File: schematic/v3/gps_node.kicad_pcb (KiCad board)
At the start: 2 copper layers, 48 x 75 mm, 81 parts, among them IC1 MCP73831/2, J1 Mounting Hole, J11 AVR ICSP, J12 UART RF, J13 LIPO_BAT, J15 UART GPS, J16 FW_UPDATE, J17 u.FL connector, J2 Mounting Hole, J3 Mounting Hole, J4 Mounting Hole, J5 TEST Vbatt, J6 USB_OTG, J7 Test 3.3v, J8 Test Gnd, J9 Test V_bak, SW1 RS stock no. 448-0747, SW2 SW_Push, SW3 SW_Push, U1 TLV71333PDBV, U2 ublox-cam-m8q-0, U3 TLV71333PDBV, U4 ATMEGA32U4-AU, U5 RN2483, U6 LIS3DH, Y1 16MHz

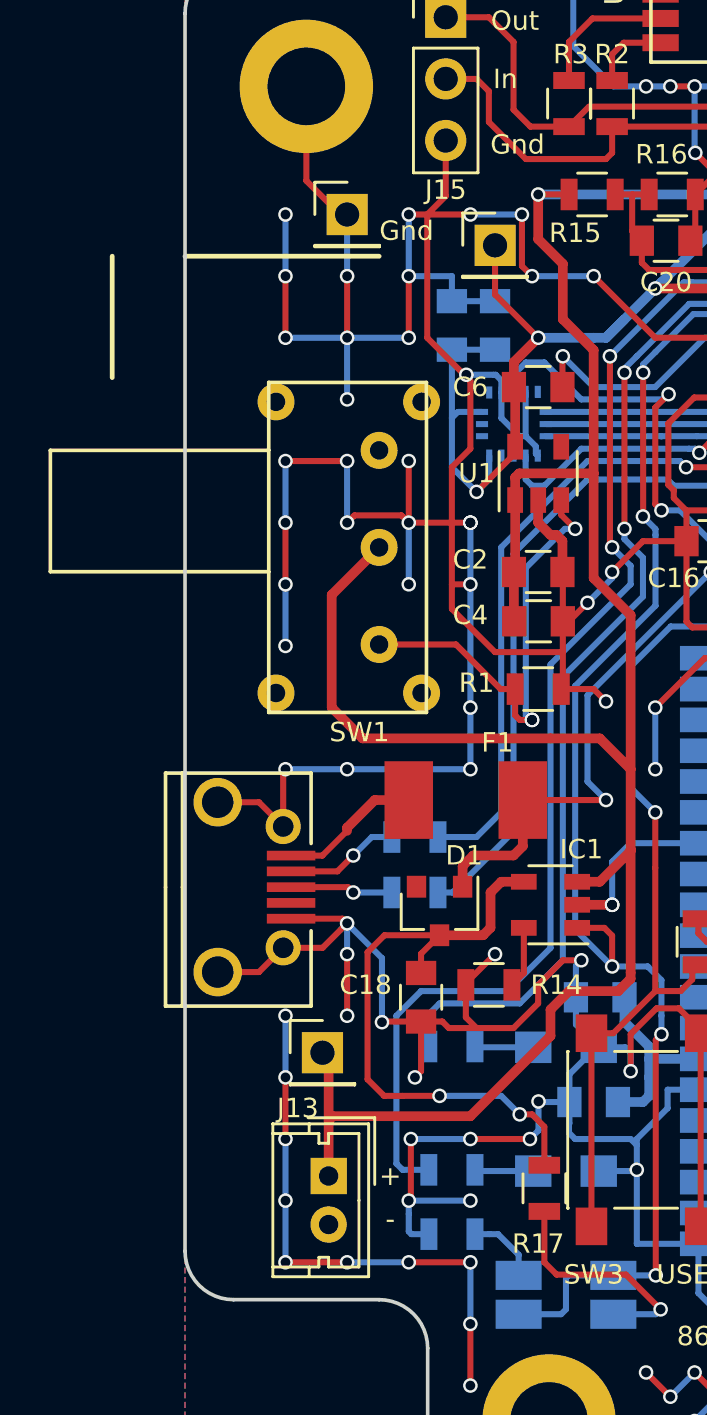
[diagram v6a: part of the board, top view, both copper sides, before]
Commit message: Moved usb connector
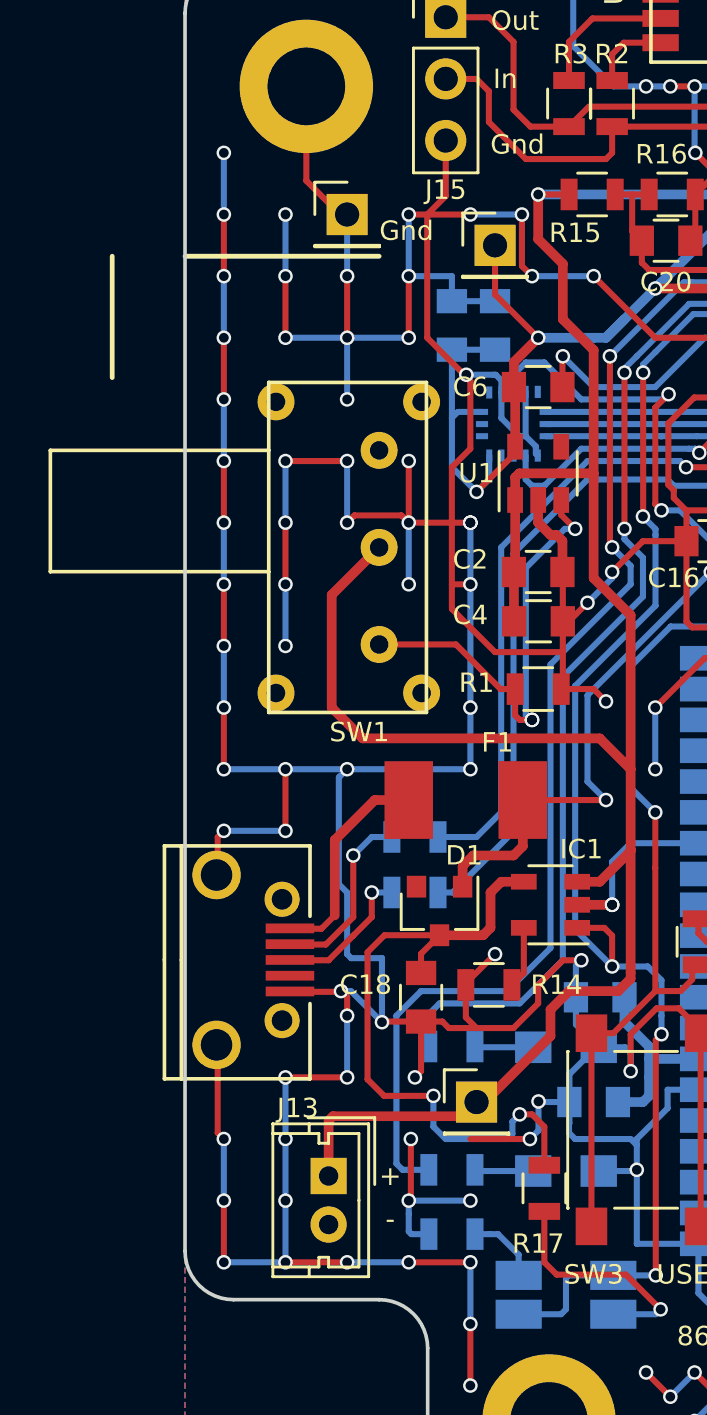
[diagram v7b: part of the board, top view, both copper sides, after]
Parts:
- moved J5 6.67 mm to (112.0, 117.9)
- moved J6 3.00 mm to (104.0, 112.0)
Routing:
- net GND: track 776.7 -> 817.9 mm, vias 230 -> 244
- net V_BATT: track 124.3 -> 116.6 mm
- net Net-(F1-Pad2): track 5.87 -> 8.86 mm
- net Net-(J6-Pad2): track 4.74 -> 7.48 mm
- net /power/V_Charger: track 25.3 -> 27.2 mm
- net Net-(J6-Pad3): track 4.24 -> 5.91 mm

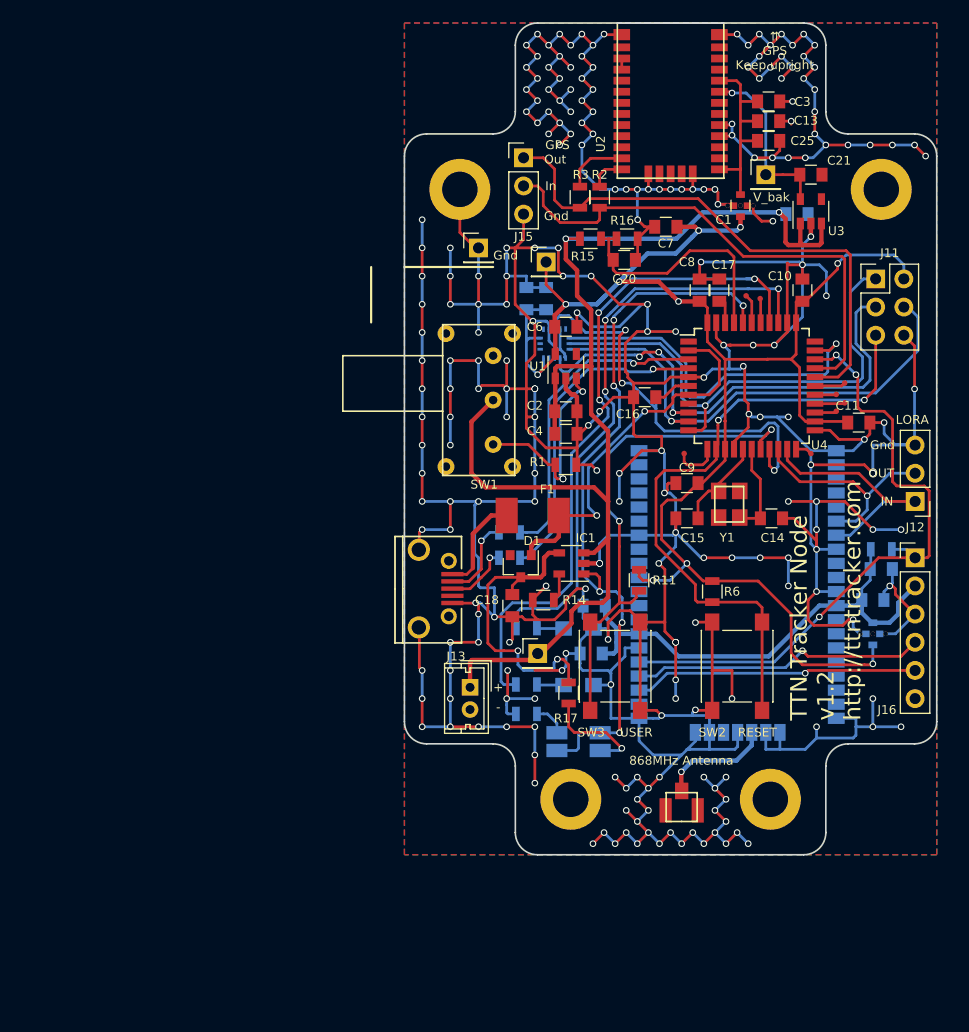
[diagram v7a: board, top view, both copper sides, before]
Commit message: Updated layout to revised schematic, moved switch and usb
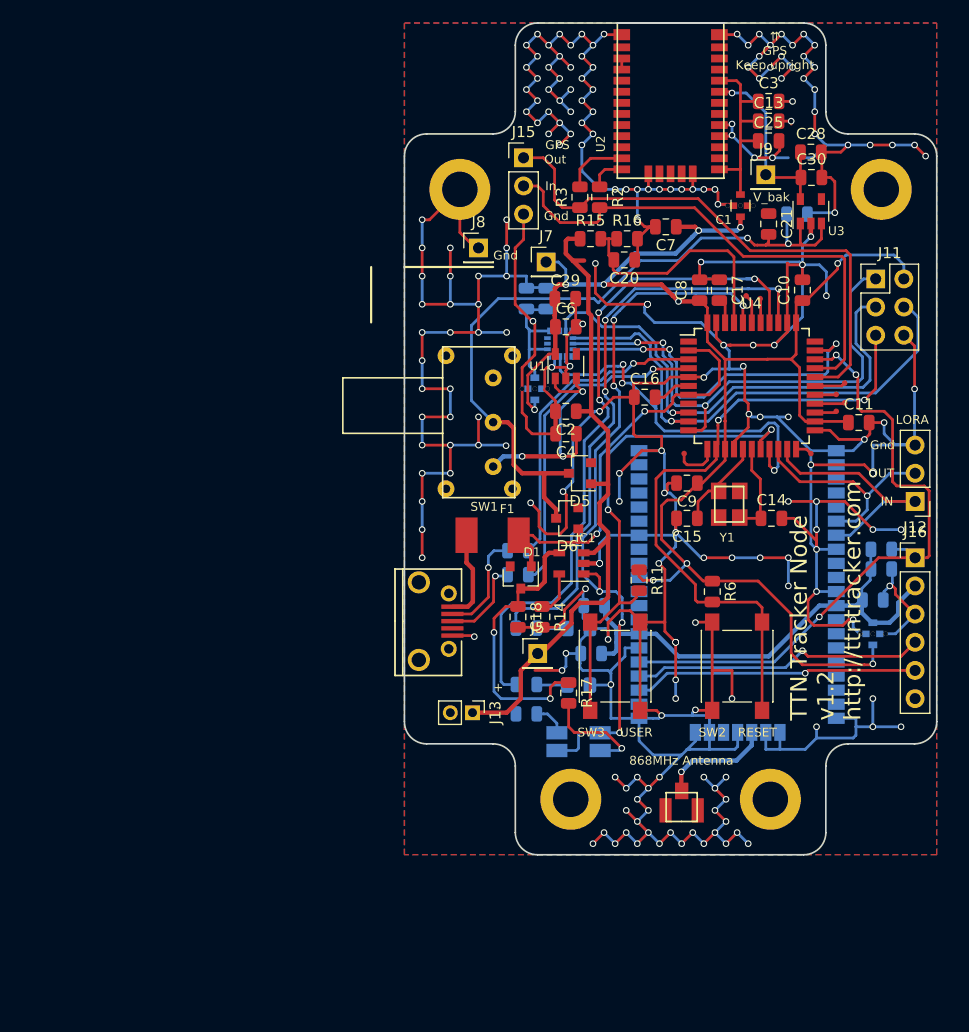
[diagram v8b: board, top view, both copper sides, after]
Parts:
- removed R1: 10k, Resistors_SMD:R_0805
- added C28: 100nF, Capacitor_SMD:C_0805_2012Metric, F.Cu at (136.7, 72.6)
- added C29: 100nF, Capacitor_SMD:C_0805_2012Metric, F.Cu at (114.5, 85.9)
- added C30: 4.7uF, Capacitor_SMD:C_0805_2012Metric, F.Cu at (136.7, 74.9)
- added C31: C_Feedthrough, gps_node_components:C_FEEDTHROUGH_0805, B.Cu at (111.8, 94.0)
- added D5: BAS K73, Diode_SMD:D_SOT-23_ANK, F.Cu at (115.8, 101.6)
- added D6: BAS K73, Diode_SMD:D_SOT-23_ANK, F.Cu at (114.7, 105.7)
- C10, C11, C12, C13, C14, C15, C16, C17, C20, C22, C23, C24, C25, C27, C4, C7, C8, C9: footprint Capacitors_SMD:C_0805 -> Capacitor_SMD:C_0805_2012Metric
- C18, C2, C26, C3, C5, C6: value 10uF -> 4.7uF; footprint Capacitors_SMD:C_0805 -> Capacitor_SMD:C_0805_2012Metric
- C21: value 100nF -> 4.7uF; footprint Capacitors_SMD:C_0805 -> Capacitor_SMD:C_0805_2012Metric
- D1: footprint Diodes_SMD:D_SOT-23_ANK -> Diode_SMD:D_SOT-23_ANK
- D3, D4: footprint LEDs:LED_0805_HandSoldering -> LED_SMD:LED_0805_2012Metric_Pad1.15x1.40mm_HandSolder
- IC1, U1, U3: footprint TO_SOT_Packages_SMD:SOT-23-5 -> Package_TO_SOT_SMD:SOT-23-5
- J1, J2, J3, J4: footprint Mounting_Holes:MountingHole_3.2mm_M3_ISO14580_Pad -> MountingHole:MountingHole_3.2mm_M3_ISO14580_Pad
- J11: footprint Pin_Headers:Pin_Header_Straight_2x03_Pitch2.54mm -> Connector_PinHeader_2.54mm:PinHeader_2x03_P2.54mm_Vertical
- J12, J15: footprint Pin_Headers:Pin_Header_Straight_1x03_Pitch2.54mm -> Connector_PinHeader_2.54mm:PinHeader_1x03_P2.54mm_Vertical
- J13: footprint Connectors_Molex:Molex_MicroLatch-53253-0270_02x2.00mm_Straight -> Connector_PinHeader_2.00mm:PinHeader_1x02_P2.00mm_Vertical
- J16: footprint Pin_Headers:Pin_Header_Straight_1x06_Pitch2.54mm -> Connector_PinHeader_2.54mm:PinHeader_1x06_P2.54mm_Vertical
- J5, J7, J8, J9: footprint Socket_Strips:Socket_Strip_Straight_1x01_Pitch2.54mm -> Connector_PinHeader_2.54mm:PinHeader_1x01_P2.54mm_Vertical
- R10, R11, R12, R13, R14, R15, R16, R17, R18, R2, R3, R4, R5, R6: footprint Resistors_SMD:R_0805 -> Resistor_SMD:R_0805_2012Metric
- SW1: value RS stock no. 448-0747 -> Switch
- SW2, SW3: footprint Buttons_Switches_SMD:SW_SPST_PTS645 -> Button_Switch_SMD:SW_SPST_PTS645
- U4: footprint Housings_QFP:TQFP-44_10x10mm_Pitch0.8mm -> Package_QFP:TQFP-44_10x10mm_P0.8mm
- U6: footprint lga_16:LGA16-pitch0.5-3mmx3mm -> Package_LGA:LGA-16_3x3mm_P0.5mm_LayoutBorder3x5y
- moved C21 5.85 mm to (132.8, 79.1), turned to 270 degrees
- moved F1 4.03 mm to (108.0, 107.2)
- moved J6 2.94 mm to (104.0, 114.9)
- moved J13 2.30 mm to (106.1, 123.2)
- moved SW1 2.00 mm to (108.0, 97.0)
- moved R5 1.82 mm to (110.2, 108.6)
- moved R4 1.70 mm to (110.2, 110.7)
- moved R14 1.53 mm to (112.4, 114.6), turned to 270 degrees
- moved C18 1.14 mm to (110.2, 114.6)
- moved D1 1.02 mm to (110.5, 111.0)
- moved U6 0.51 mm to (114.0, 89.9)
- turned C14 to 0 degrees
- turned C15 to 180 degrees
- turned C2 to 180 degrees
- turned C4 to 180 degrees
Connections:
- C14 pad 1: GND -> Net-(C14-Pad1)
- C14 pad 2: Net-(C14-Pad2) -> GND
- C15 pad 1: GND -> Net-(C15-Pad1)
- C15 pad 2: Net-(C15-Pad2) -> GND
- C21 pad 1: V_BAK -> GND
- C21 pad 2: GND -> /power/V_BAK_SUPPLY
- C22 pad 1: V_BATT -> /power/V_BAK_SUPPLY
- C26 pad 1: V_3.3 -> /accelerometer/ACCEL_POWER
- C27 pad 1: V_3.3 -> /accelerometer/ACCEL_POWER
- C4 pad 1: V_BATT -> /power/V3.3_SUPPLY
- J16 pad 6: (no net) -> Net-(J16-Pad6)
- J6 pad 4: (no net) -> Net-(J6-Pad4)
- SW1 pad 1: (no net) -> Net-(SW1-Pad1)
- SW1 pad 2: V_BATT -> /power/V_BAK_SUPPLY
- SW1 pad 3: /power/REG_ENABLE -> /power/V3.3_SUPPLY
- U1 pad 1: V_BATT -> /power/V3.3_SUPPLY
- U1 pad 3: /power/REG_ENABLE -> /power/V3.3_SUPPLY
- U1 pad 4: (no net) -> Net-(U1-Pad4)
- U2 pad 2: (no net) -> Net-(U2-Pad2)
- U2 pad 20: (no net) -> Net-(U2-Pad20)
- U2 pad 23: (no net) -> Net-(U2-Pad23)
- U2 pad 24: (no net) -> Net-(U2-Pad24)
- U2 pad 28: (no net) -> Net-(U2-Pad28)
- U2 pad 29: (no net) -> Net-(U2-Pad29)
- U2 pad 3: (no net) -> Net-(U2-Pad3)
- U2 pad 30: (no net) -> Net-(U2-Pad30)
- U2 pad 6: (no net) -> Net-(U2-Pad6)
- U2 pad 7: (no net) -> Net-(U2-Pad7)
- U3 pad 1: V_BATT -> /power/V_BAK_SUPPLY
- U3 pad 3: V_BATT -> /power/V_BAK_SUPPLY
- U3 pad 4: (no net) -> Net-(U3-Pad4)
- U4 pad 1: (no net) -> Net-(U4-Pad1)
- U4 pad 16: Net-(C15-Pad2) -> Net-(C15-Pad1)
- U4 pad 17: Net-(C14-Pad2) -> Net-(C14-Pad1)
- U4 pad 33: (no net) -> Net-(U4-Pad33)
- U4 pad 8: (no net) -> Net-(U4-Pad8)
- U5 pad 10: (no net) -> Net-(U5-Pad10)
- U5 pad 13: (no net) -> Net-(U5-Pad13)
- U5 pad 14: (no net) -> Net-(U5-Pad14)
- U5 pad 15: (no net) -> Net-(U5-Pad15)
- U5 pad 16: (no net) -> Net-(U5-Pad16)
- U5 pad 17: (no net) -> Net-(U5-Pad17)
- U5 pad 18: (no net) -> Net-(U5-Pad18)
- U5 pad 19: (no net) -> Net-(U5-Pad19)
- U5 pad 2: (no net) -> Net-(U5-Pad2)
- U5 pad 25: (no net) -> Net-(U5-Pad25)
- U5 pad 29: (no net) -> Net-(U5-Pad29)
- U5 pad 3: (no net) -> Net-(U5-Pad3)
- U5 pad 35: (no net) -> Net-(U5-Pad35)
- U5 pad 36: (no net) -> Net-(U5-Pad36)
- U5 pad 37: (no net) -> Net-(U5-Pad37)
- U5 pad 38: (no net) -> Net-(U5-Pad38)
- U5 pad 39: (no net) -> Net-(U5-Pad39)
- U5 pad 4: (no net) -> Net-(U5-Pad4)
- U5 pad 40: (no net) -> Net-(U5-Pad40)
- U5 pad 42: (no net) -> Net-(U5-Pad42)
- U5 pad 43: (no net) -> Net-(U5-Pad43)
- U5 pad 44: (no net) -> Net-(U5-Pad44)
- U5 pad 45: (no net) -> Net-(U5-Pad45)
- U5 pad 46: (no net) -> Net-(U5-Pad46)
- U5 pad 5: (no net) -> Net-(U5-Pad5)
- U5 pad 9: (no net) -> Net-(U5-Pad9)
- U6 pad 1: V_3.3 -> /accelerometer/ACCEL_POWER
- U6 pad 13: (no net) -> Net-(U6-Pad13)
- U6 pad 14: V_3.3 -> /accelerometer/ACCEL_POWER
- U6 pad 15: (no net) -> Net-(U6-Pad15)
- U6 pad 16: (no net) -> Net-(U6-Pad16)
- U6 pad 2: (no net) -> Net-(U6-Pad2)
- U6 pad 3: (no net) -> Net-(U6-Pad3)
- U6 pad 9: (no net) -> Net-(U6-Pad9)
- Y1 pad 1: Net-(C14-Pad2) -> Net-(C14-Pad1)
- Y1 pad 2: Net-(C15-Pad2) -> Net-(C15-Pad1)
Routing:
- net GND: track 817.9 -> 735.1 mm, vias 244 -> 211
- net /power/V_BAK_SUPPLY: track 0.00 -> 68.0 mm, vias 0 -> 2
- net V_BATT: track 116.6 -> 61.6 mm, vias 2 -> 0
- net /power/V3.3_SUPPLY: track 0.00 -> 21.6 mm, vias 0 -> 3
- net /power/REG_ENABLE: track 18.8 -> 0.00 mm, vias 3 -> 0
- net /accelerometer/ACCEL_POWER: track 0.00 -> 11.7 mm
- net Net-(C14-Pad2): track 8.45 -> 0.00 mm
- net Net-(C14-Pad1): track 0.00 -> 8.45 mm
- net Net-(C15-Pad2): track 8.44 -> 0.00 mm
- net Net-(C15-Pad1): track 0.00 -> 8.44 mm
- net V_3.3: track 147.5 -> 141.9 mm
- net V_BUS: track 34.1 -> 38.3 mm
- net /Microcontroller/ACCEL_INT: track 37.0 -> 33.0 mm
- net V_BAK: track 15.9 -> 18.2 mm
- net Net-(J6-Pad3): track 5.91 -> 7.97 mm
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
